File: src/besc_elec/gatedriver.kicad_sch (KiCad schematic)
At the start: 31 parts, among them U201 DRV8301

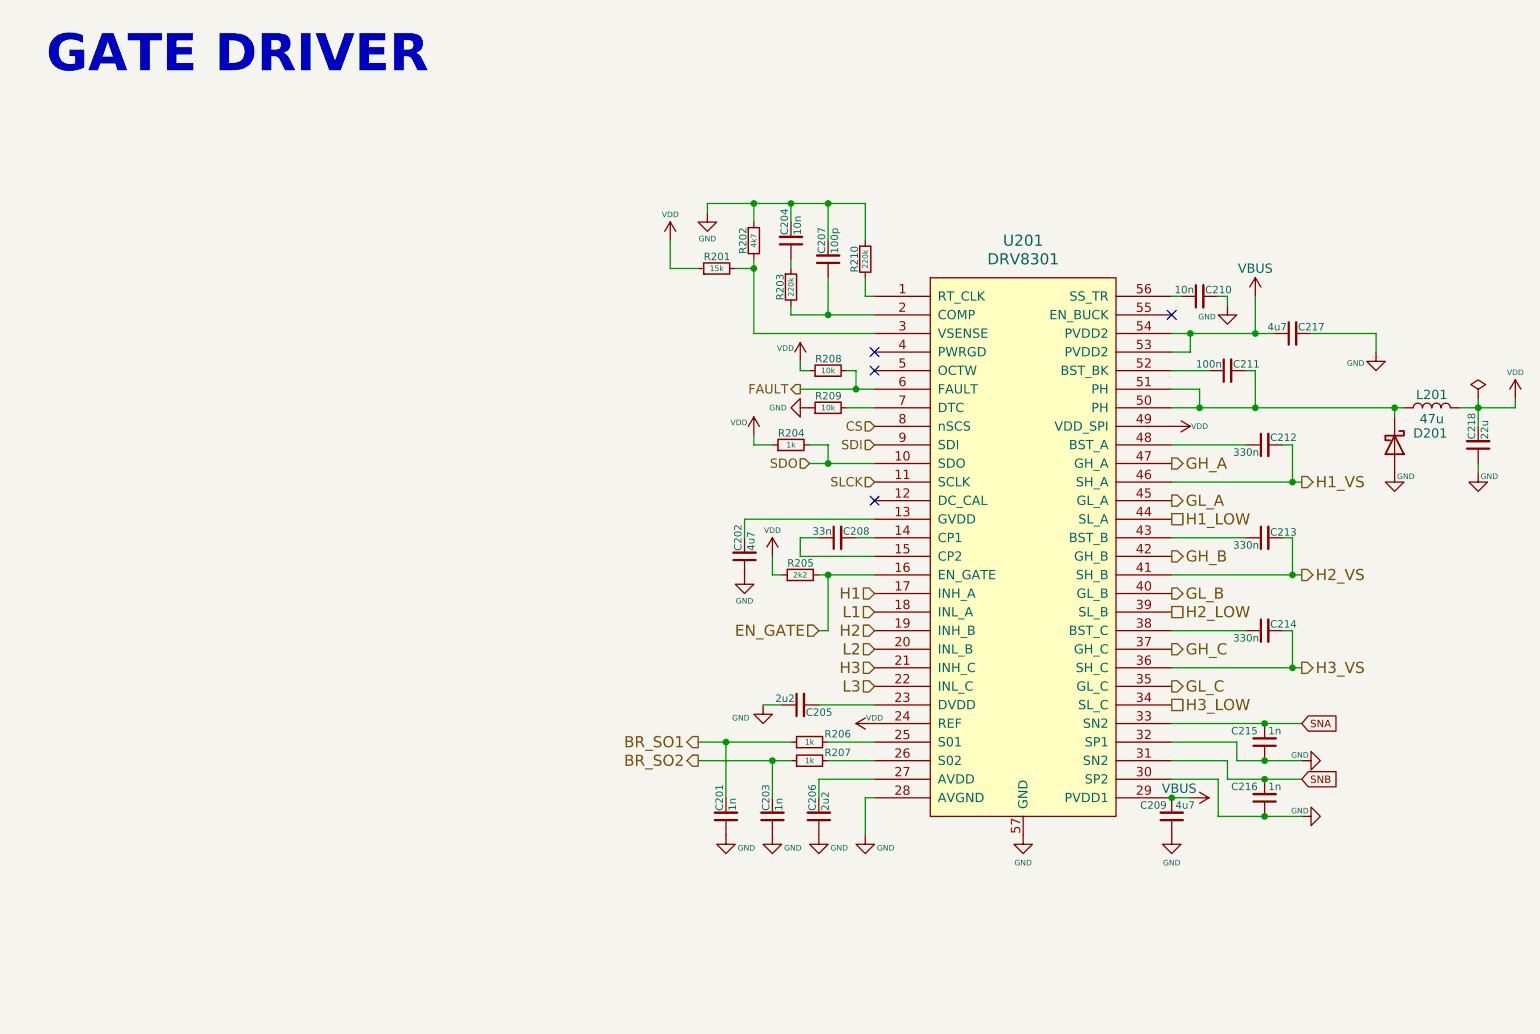
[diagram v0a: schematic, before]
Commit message: added DRV8323HRTAR symbol and footprint
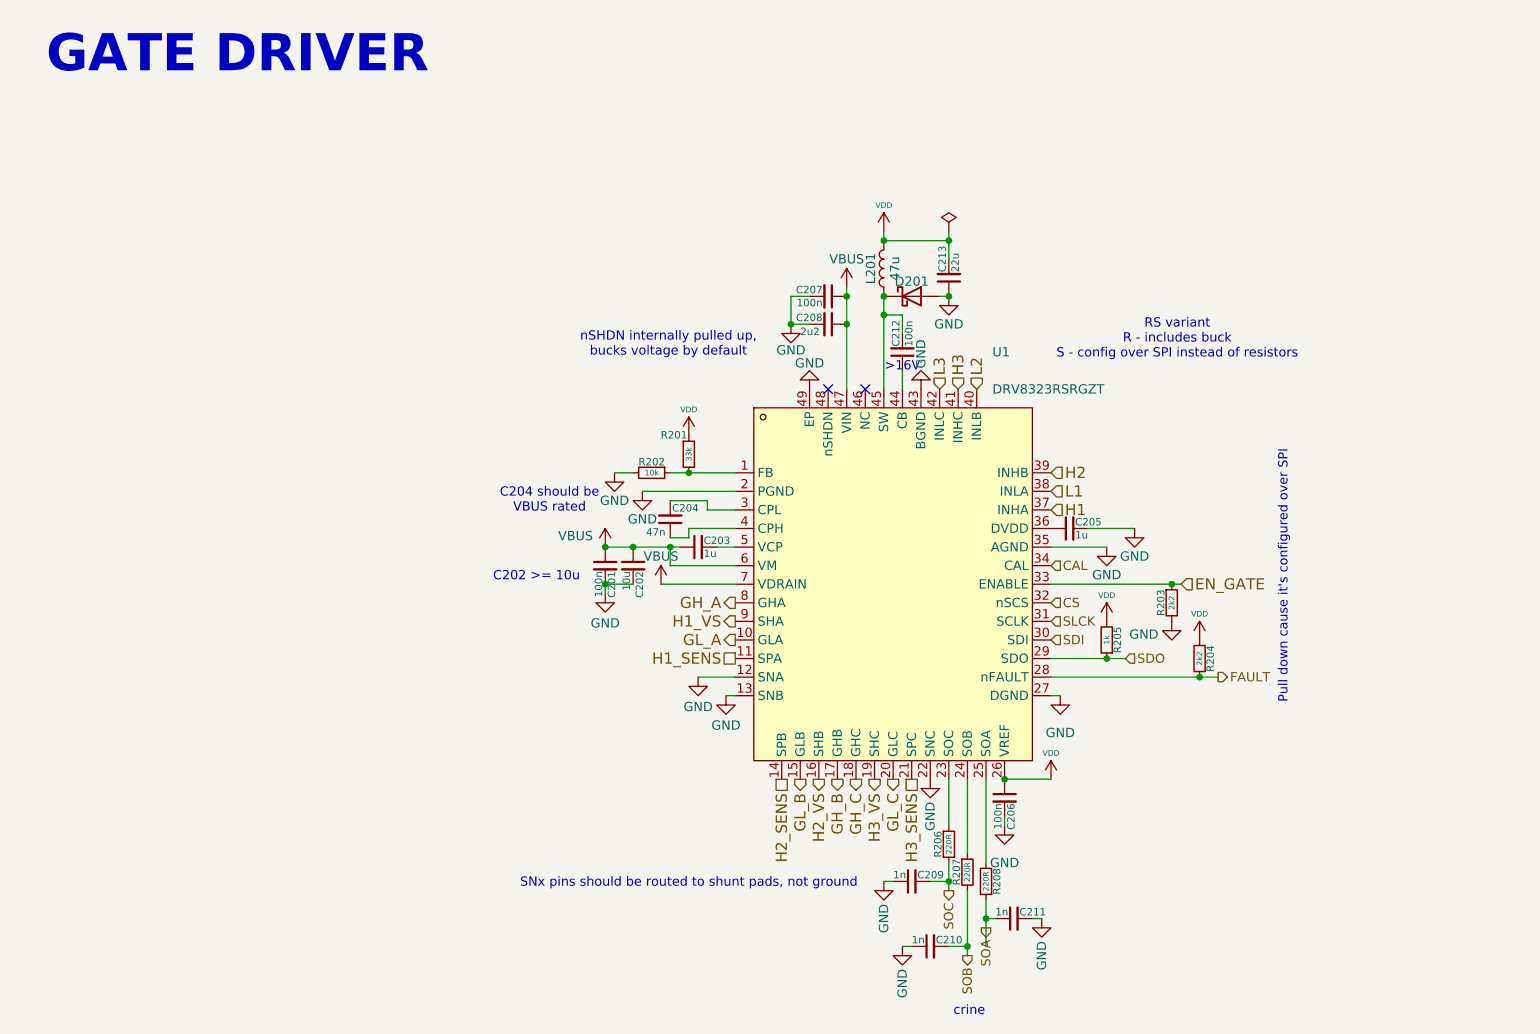
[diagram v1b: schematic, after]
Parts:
- removed C205: 2u2, Capacitor_SMD:C_0603_1608Metric, symbol Bluesat:C_CompactH
- removed C208: 33n, Capacitor_SMD:C_0603_1608Metric, symbol Bluesat:C_CompactH
- removed C209: 4u7, Capacitor_SMD:C_1210_3225Metric, symbol Bluesat:C_CompactV
- removed C212, C213, C214: 330n, Capacitor_SMD:C_0603_1608Metric, symbol Bluesat:C_CompactH
- removed C215, C216: 1n, Capacitor_SMD:C_0402_1005Metric, symbol Bluesat:C_CompactV
- removed C217: 4u7, Capacitor_SMD:C_1210_3225Metric, symbol Bluesat:C_CompactH
- removed C218: 22u, Capacitor_SMD:C_1210_3225Metric, symbol Bluesat:C_CompactV
- removed R201: 15k, Resistor_SMD:R_0402_1005Metric, symbol Bluesat:R_CompactH
- removed R204, R206, R207: 1k, Resistor_SMD:R_0402_1005Metric, symbol Bluesat:R_CompactH
- removed R205: 2k2, Resistor_SMD:R_0402_1005Metric, symbol Bluesat:R_CompactH
- removed R208, R209: 10k, Resistor_SMD:R_0402_1005Metric, symbol Bluesat:R_CompactH
- removed R210: 220k, Resistor_SMD:R_0402_1005Metric, symbol Bluesat:R_CompactV
- removed U201: DRV8301, Bluesat:HTSSOP-56_6.1x14-0.5-EP, symbol Bluesat:DRV8301
- added C205: 1u, symbol Bluesat:C_CompactV
- added C208: 2u2, symbol Bluesat:C_CompactV
- added C209: 1n, symbol Bluesat:C_CompactH
- added C212: 100n, Capacitor_SMD:C_1210_3225Metric, symbol Bluesat:C_CompactV
- added C213: 22u, Capacitor_SMD:C_1210_3225Metric, symbol Bluesat:C_CompactV
- added R201: 33k, symbol Bluesat:R_CompactV
- added R204: 2k2, symbol Bluesat:R_CompactV
- added R205: 1k, symbol Bluesat:R_CompactV
- added R206, R207, R208: 220R, symbol Bluesat:R_CompactV
- added U1: DRV8323RSRGZT, easyeda2kicad:VQFN-48_L7.0-W7.0-P0.50-BL-EP5.5, symbol easyeda2kicad:DRV8323RSRGZT
- C201: value 1n -> 100n; footprint Capacitor_SMD:C_0402_1005Metric -> (none)
- C202: value 4u7 -> 10u; footprint Capacitor_SMD:C_1206_3216Metric -> (none)
- C203: value 1n -> 1u; footprint Capacitor_SMD:C_0402_1005Metric -> (none)
- C204: value 10n -> 47n; footprint Capacitor_SMD:C_0402_1005Metric -> (none)
- C206: value 2u2 -> 100n; footprint Capacitor_SMD:C_0603_1608Metric -> (none)
- C207: value 100p -> 100n; footprint Capacitor_SMD:C_0402_1005Metric -> (none)
- C210: value 10n -> 1n; footprint Capacitor_SMD:C_0402_1005Metric -> (none)
- C211: value 100n -> 1n; footprint Capacitor_SMD:C_0603_1608Metric -> (none)
- R202: value 4k7 -> 10k; footprint Resistor_SMD:R_0402_1005Metric -> (none)
- R203: value 220k -> 2k2; footprint Resistor_SMD:R_0402_1005Metric -> (none)
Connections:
- net BR_SO1 is gone; now on net GND: C201.2
- net CS: now also U1.32 (nSCS)
- net EN_GATE: now also R203.1, U1.33 (ENABLE)
- net FAULT: now also R204.1, U1.28 (nFAULT)
- net GH_A: now also U1.8 (GHA)
- net GH_B: now also U1.17 (GHB)
- net GH_C: now also U1.18 (GHC)
- net GL_A: now also U1.10 (GLA)
- net GL_B: now also U1.15 (GLB)
- net GL_C: now also U1.20 (GLC)
- net GND: now also C202.2, C206.2, C210.1, C211.2, R202.2, R203.2, C205.2, C208.2, C209.1, C213.1, U1.12 (SNA), U1.13 (SNB), U1.2 (PGND), U1.22 (SNC), U1.27 (DGND), U1.35 (AGND), U1.43 (BGND), U1.49 (EP); no longer C201.1, C202.1, C203.1, C204.2, C206.1, C210.2, R202.1
- net H1: now also U1.37 (INHA)
- net H1_VS: now also U1.9 (SHA)
- net H2: now also U1.39 (INHB)
- net H2_VS: now also U1.16 (SHB)
- net H3: now also U1.41 (INHC)
- net H3_VS: now also U1.19 (SHC)
- net L1: now also U1.38 (INLA)
- net L2: now also U1.40 (INLB)
- net L3: now also U1.42 (INLC)
- net SDI: now also U1.30 (SDI)
- net SDO: now also R205.1, U1.29 (SDO)
- net SLCK: now also U1.31 (SCLK)
- net VBUS: now also C201.1, C202.1, C203.1, C207.1, C208.1, U1.47 (VIN), U1.6 (VM), U1.7 (VDRAIN)
- net VDD: now also C206.1, C213.2, R201.1, R204.2, R205.2, U1.26 (VREF)
- net at D201.1 (K), L201.1: now also C212.2, U1.45 (SW); no longer C211.2
- net at C204.1: now also U1.4 (CPH); no longer R203.1
- net SOA: now reaches C211.1
- net SOA: now also R208.1
- net BR_SO2: no longer names the net of C203.2
- net BR_SO2: now also U1.5 (VCP)
- new net: R201.2, R202.1, U1.1 (FB)
- new net: C204.2, U1.3 (CPL)
- new net: R206.1, U1.23 (SOC)
- new net: R207.1, U1.24 (SOB)
- new net: R208.2, U1.25 (SOA)
- new net: C205.1, U1.36 (DVDD)
- new net: C212.1, U1.44 (CB)
- new net CAL: U1.34 (CAL)
- new net H1_SENS: U1.11 (SPA)
- new net H2_SENS: U1.14 (SPB)
- new net H3_SENS: U1.21 (SPC)
- new net SOB: C210.2, R207.2
- new net SOC: C209.2, R206.2
- no-connect marks 4 -> 2
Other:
- note added: ">16V"
- note added: "C202 >= 10u"
- note added: "C204 should be VBUS rated"
- note added: "Pull down cause it's configured over SPI"
- note added: "RS variant R - includes buck S - config over SPI instead of resistors"
- note added: "SNx pins should be routed to shunt pads, not ground"
- note added: "crine"
- note added: "nSHDN internally pulled up, bucks voltage by default"

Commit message: switched gate driver variant from RS->HR
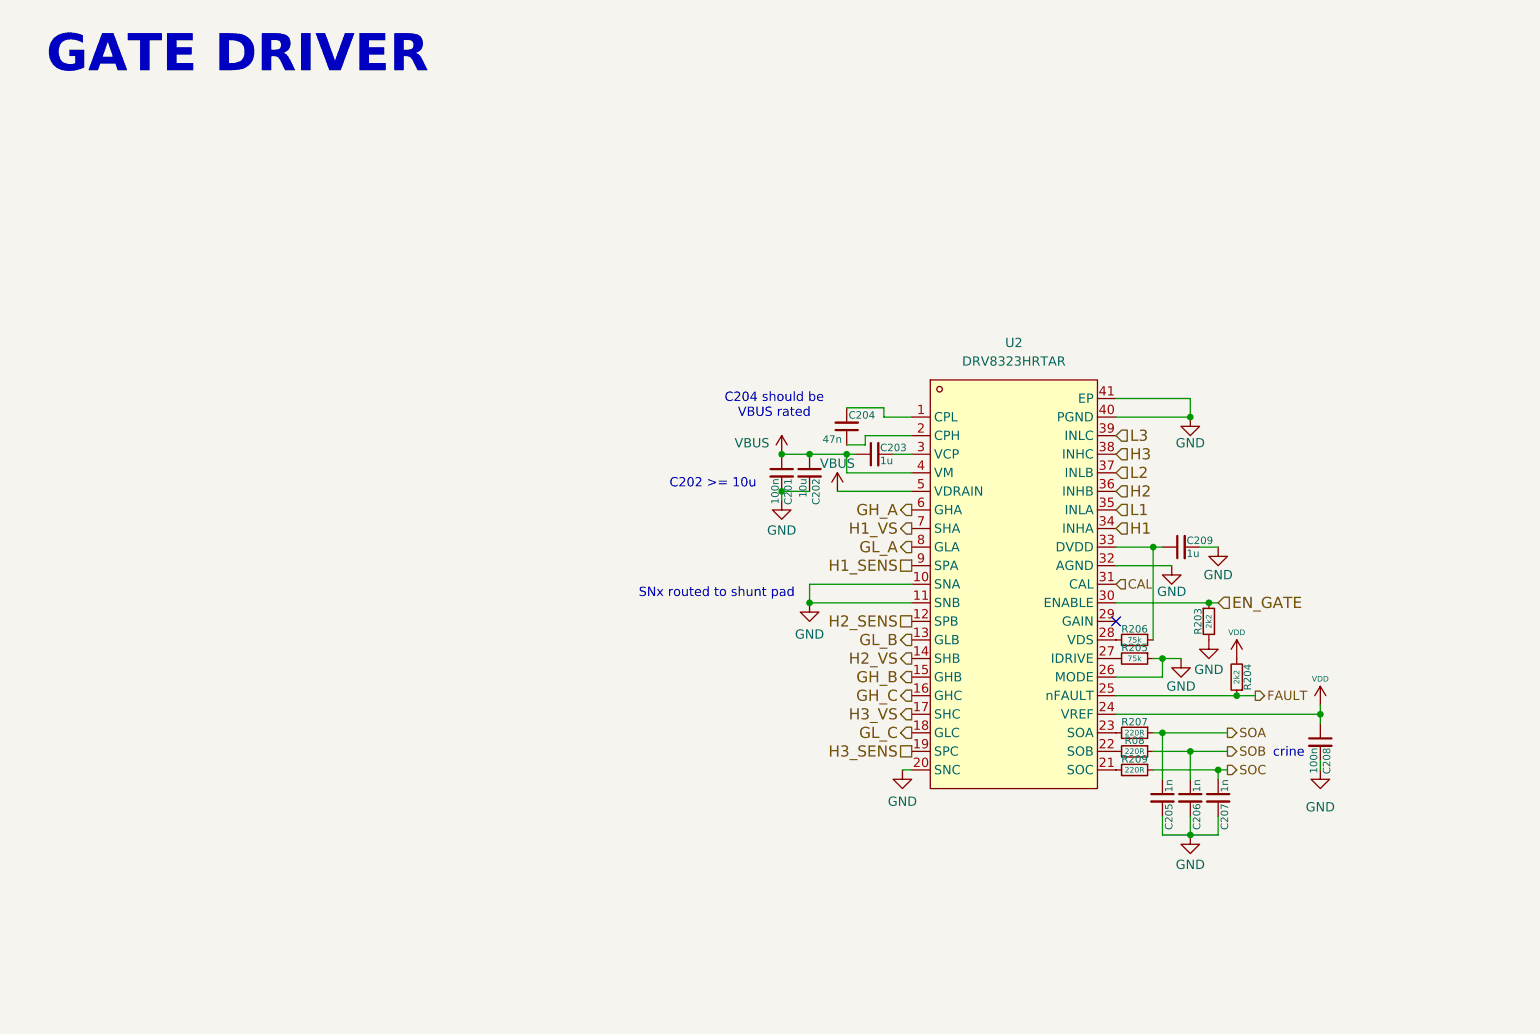
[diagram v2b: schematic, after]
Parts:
- removed C206, C207: 100n, symbol Bluesat:C_CompactV
- removed C209, C210, C211: 1n, symbol Bluesat:C_CompactH
- removed C212: 100n, Capacitor_SMD:C_1210_3225Metric, symbol Bluesat:C_CompactV
- removed C213: 22u, Capacitor_SMD:C_1210_3225Metric, symbol Bluesat:C_CompactV
- removed D201: D_Schottky, Diode_SMD:D_SOD-123, symbol Device:D_Schottky
- removed L201: 47u, Inductor_SMD:L_Changjiang_FXL0630, symbol Device:L
- removed R201: 33k, symbol Bluesat:R_CompactV
- removed R202: 10k, symbol Bluesat:R_CompactV
- removed R208: 220R, symbol Bluesat:R_CompactV
- removed U1: DRV8323RSRGZT, easyeda2kicad:VQFN-48_L7.0-W7.0-P0.50-BL-EP5.5, symbol easyeda2kicad:DRV8323RSRGZT
- added C205, C206, C207: 1n, symbol Bluesat:C_CompactH
- added R08, R209: 220R, symbol Bluesat:R_CompactV
- added U2: DRV8323HRTAR, besc:QFN-40_L6.0-W6.0-P0.50-BL-EP4.5, symbol besc:DRV8323HRTAR
- C208: value 2u2 -> 100n
- R205: value 1k -> 75k
- R206: value 220R -> 75k
- renumbered C205 to C209
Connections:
- net SDO is gone; now on net GND: R205.1
- net CAL: now also U2.31 (CAL)
- net EN_GATE: now also U2.30 (ENABLE)
- net FAULT: now also U2.25 (nFAULT)
- net GH_A: now also U2.6 (GHA)
- net GH_B: now also U2.15 (GHB)
- net GH_C: now also U2.16 (GHC)
- net GL_A: now also U2.8 (GLA)
- net GL_B: now also U2.13 (GLB)
- net GL_C: now also U2.18 (GLC)
- net GND: now also C205.2, C206.2, C207.2, U2.10 (SNA), U2.11 (SNB), U2.20 (SNC), U2.26 (MODE), U2.32 (AGND), U2.40 (PGND), U2.41 (EP)
- net H1: now also U2.34 (INHA)
- net H1_SENS: now also U2.9 (SPA)
- net H1_VS: now also U2.7 (SHA)
- net H2: now also U2.36 (INHB)
- net H2_SENS: now also U2.12 (SPB)
- net H2_VS: now also U2.14 (SHB)
- net H3: now also U2.38 (INHC)
- net H3_SENS: now also U2.19 (SPC)
- net H3_VS: now also U2.17 (SHC)
- net L1: now also U2.35 (INLA)
- net L2: now also U2.37 (INLB)
- net L3: now also U2.39 (INLC)
- net SOA: now also R207.1, C205.1
- net SOB: now also C206.1, R08.1; no longer R207.2
- net SOC: now also C207.1, R209.1; no longer R206.2
- net VBUS: now also U2.4 (VM), U2.5 (VDRAIN); no longer C208.1
- net VDD: now also C208.1, U2.24 (VREF); no longer R205.2
- net at C204.1: now also U2.2 (CPH)
- net at C204.2: now also U2.1 (CPL)
- net at R206.1: now also C209.1, U2.33 (DVDD)
- net at C203.2: now also U2.3 (VCP)
- new net: R205.2, U2.27 (IDRIVE)
- new net: R206.2, U2.28 (VDS)
- new net: R209.2, U2.21 (SOC)
- new net: R08.2, U2.22 (SOB)
- new net: R207.2, U2.23 (SOA)
- no-connect marks 2 -> 1
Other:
- note added: "SNx routed to shunt pad"
- note removed: ">16V"
- note removed: "Pull down cause it's configured over SPI"
- note removed: "RS variant R - includes buck S - config over SPI instead of resistors"
- note removed: "SNx pins should be routed to shunt pads, not ground"
- note removed: "nSHDN internally pulled up, bucks voltage by default"
- moved on the sheet: C201, C202, C203, C204, C209
